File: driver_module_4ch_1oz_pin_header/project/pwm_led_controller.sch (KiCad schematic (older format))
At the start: 35 parts, among them J1 Conn_01x05_Male, J2 Conn_01x02_Male, J3 Conn_01x02_Male, J4 Conn_01x02_Male, J5 Conn_01x02_Male, J6 Conn_01x02_Male, J7 Conn_01x02_Male, U1 AL8843, U2 AL8843, U3 AL8843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

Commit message: Проект выполнен под установку светильника
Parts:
- removed J2, J3: Conn_01x02_Male, my_lib:TerminalBlock-1x02_P5.08mm_Horizontal, symbol Connector:Conn_01x02_Male
- added J2, J3: Conn_01x04_Male, Connector_PinHeader_2.54mm:PinHeader_1x04_P2.54mm_Vertical, symbol Connector:Conn_01x04_Male
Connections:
- net +15V: now also J2.1 (Pin_1), J2.2 (Pin_2)
- net +28V: now also J3.1 (Pin_1), J3.2 (Pin_2)
- net GND: now also J2.3 (Pin_3), J2.4 (Pin_4), J3.3 (Pin_3), J3.4 (Pin_4)
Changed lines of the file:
@@
 L power:+15V #PWR0102
 U 1 1 5C9EEA26
-P 13850 2550
-F 0 "#PWR0102" H 13850 2400 50  0001 C CNN
-F 1 "+15V" H 13865 2723 50  0000 C CNN
-F 2 "" H 13850 2550 50  0001 C CNN
-F 3 "" H 13850 2550 50  0001 C CNN
-	1    13850 2550
+P 15000 2550
+F 0 "#PWR0102" H 15000 2400 50  0001 C CNN
+F 1 "+15V" H 15015 2723 50  0000 C CNN
+F 2 "" H 15000 2550 50  0001 C CNN
+F 3 "" H 15000 2550 50  0001 C CNN
+	1    15000 2550
 	1    0    0    -1
 $EndComp
@@
 L power:GND #PWR0101
 U 1 1 5C9F6278
-P 13850 2650
-F 0 "#PWR0101" H 13850 2400 50  0001 C CNN
-F 1 "GND" H 13855 2477 50  0000 C CNN
-F 2 "" H 13850 2650 50  0001 C CNN
-F 3 "" H 13850 2650 50  0001 C CNN
-	1    13850 2650
+P 15000 2850
+F 0 "#PWR0101" H 15000 2600 50  0001 C CNN
+F 1 "GND" H 15005 2677 50  0000 C CNN
+F 2 "" H 15000 2850 50  0001 C CNN
+F 3 "" H 15000 2850 50  0001 C CNN
+	1    15000 2850
 	1    0    0    -1
 $EndComp
@@
 L power:+28V #PWR0113
 U 1 1 5CA09CB3
-P 13800 3150
-F 0 "#PWR0113" H 13800 3000 50  0001 C CNN
-F 1 "+28V" H 13815 3323 50  0000 C CNN
-F 2 "" H 14050 3200 50  0001 C CNN
-F 3 "" H 14050 3200 50  0001 C CNN
-	1    13800 3150
+P 15000 3600
+F 0 "#PWR0113" H 15000 3450 50  0001 C CNN
+F 1 "+28V" H 15015 3773 50  0000 C CNN
+F 2 "" H 15250 3650 50  0001 C CNN
+F 3 "" H 15250 3650 50  0001 C CNN
+	1    15000 3600
 	1    0    0    -1
 $EndComp
@@
 $EndComp
 $Comp
-L Connector:Conn_01x02_Male J2
-U 1 1 5CA0A8BF
-P 13300 2550
-F 0 "J2" H 13406 2728 50  0000 C CNN
-F 1 "Conn_01x02_Male" H 13406 2637 50  0000 C CNN
-F 2 "my_lib:TerminalBlock-1x02_P5.08mm_Horizontal" H 13300 2550 50  0001 C CNN
-F 3 "~" H 13300 2550 50  0001 C CNN
-	1    13300 2550
-	1    0    0    -1
-$EndComp
-Wire Wire Line
-	13850 2550 13500 2550
-Wire Wire Line
-	13850 2650 13500 2650
-$Comp
-L power:GND #PWR?
+L power:GND #PWR0111
 U 1 1 5CA1B763
-P 13800 3250
-F 0 "#PWR?" H 13800 3000 50  0001 C CNN
-F 1 "GND" H 13805 3077 50  0000 C CNN
-F 2 "" H 13800 3250 50  0001 C CNN
-F 3 "" H 13800 3250 50  0001 C CNN
-	1    13800 3250
-	1    0    0    -1
-$EndComp
-$Comp
-L Connector:Conn_01x02_Male J3
-U 1 1 5CA1B769
-P 13250 3150
-F 0 "J3" H 13356 3328 50  0000 C CNN
-F 1 "Conn_01x02_Male" H 13356 3237 50  0000 C CNN
-F 2 "my_lib:TerminalBlock-1x02_P5.08mm_Horizontal" H 13250 3150 50  0001 C CNN
-F 3 "~" H 13250 3150 50  0001 C CNN
-	1    13250 3150
-	1    0    0    -1
-$EndComp
-Wire Wire Line
-	13800 3150 13450 3150
-Wire Wire Line
-	13800 3250 13450 3250
+P 15000 3900
+F 0 "#PWR0111" H 15000 3650 50  0001 C CNN
+F 1 "GND" H 15005 3727 50  0000 C CNN
+F 2 "" H 15000 3900 50  0001 C CNN
+F 3 "" H 15000 3900 50  0001 C CNN
+	1    15000 3900
+	1    0    0    -1
+$EndComp
+$Comp
+L Connector:Conn_01x04_Male J2
+U 1 1 5CA7A2EA
+P 14300 2650
+F 0 "J2" H 14406 2928 50  0000 C CNN
+F 1 "Conn_01x04_Male" H 14406 2837 50  0000 C CNN
+F 2 "Connector_PinHeader_2.54mm:PinHeader_1x04_P2.54mm_Vertical" H 14300 2650 50  0001 C CNN
+F 3 "~" H 14300 2650 50  0001 C CNN
+	1    14300 2650
+	1    0    0    -1
+$EndComp
+Wire Wire Line
+	15000 2550 14500 2550
+Wire Wire Line
+	14500 2550 14500 2650
+Connection ~ 14500 2550
+Wire Wire Line
+	15000 2850 14500 2850
+Wire Wire Line
+	14500 2850 14500 2750
+Connection ~ 14500 2850
+$Comp
+L Connector:Conn_01x04_Male J3
+U 1 1 5CA82437
+P 14300 3700
+F 0 "J3" H 14406 3978 50  0000 C CNN
+F 1 "Conn_01x04_Male" H 14406 3887 50  0000 C CNN
+F 2 "Connector_PinHeader_2.54mm:PinHeader_1x04_P2.54mm_Vertical" H 14300 3700 50  0001 C CNN
+F 3 "~" H 14300 3700 50  0001 C CNN
+	1    14300 3700
+	1    0    0    -1
+$EndComp
+Wire Wire Line
+	15000 3600 14500 3600
+Wire Wire Line
+	14500 3600 14500 3700
+Connection ~ 14500 3600
+Wire Wire Line
+	15000 3900 14500 3900
+Wire Wire Line
+	14500 3900 14500 3800
+Connection ~ 14500 3900
 $EndSCHEMATC

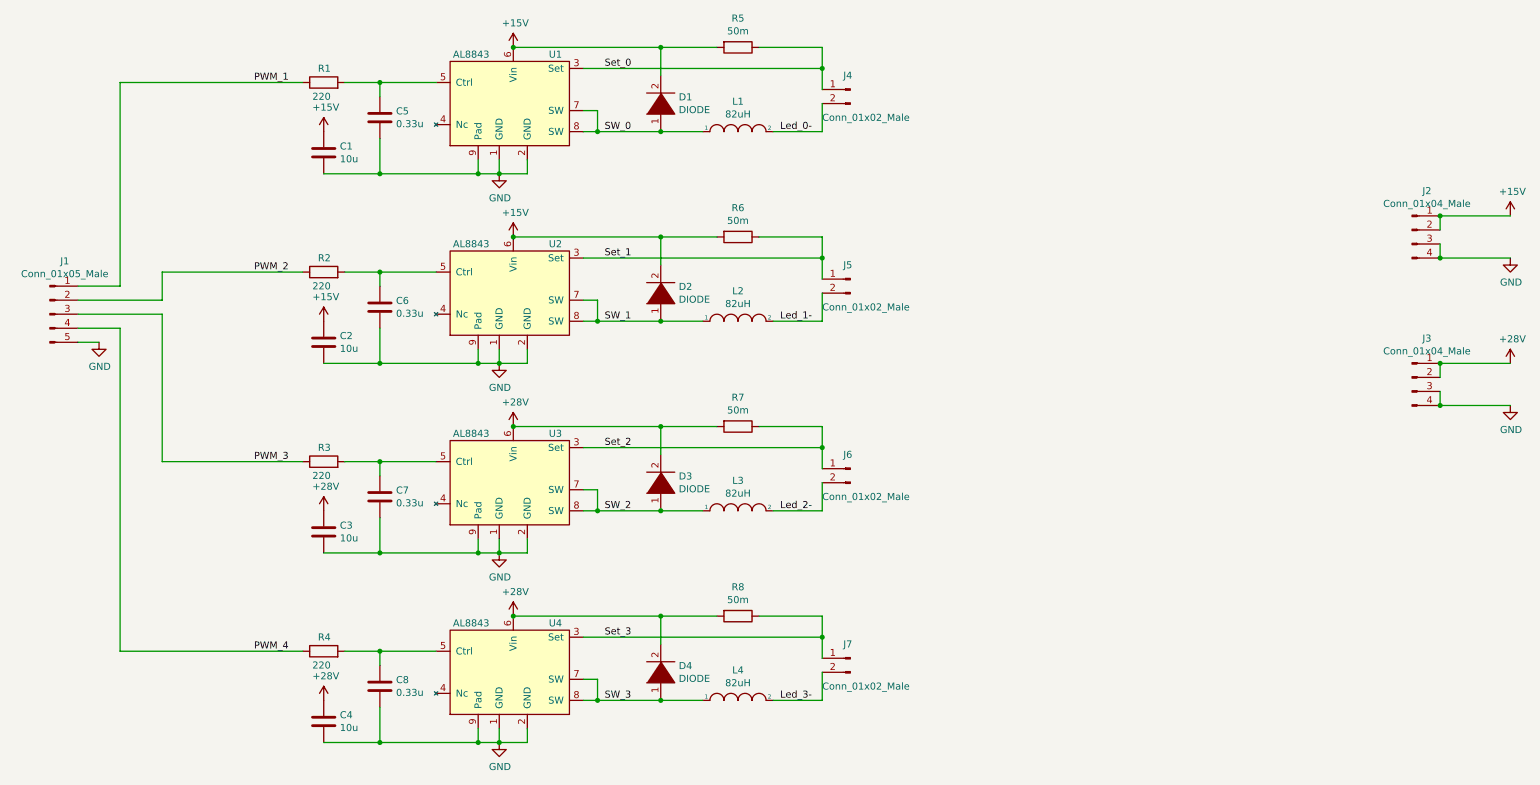
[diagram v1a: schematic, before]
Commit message: Подогнал расположение вилок под светодиодную плату
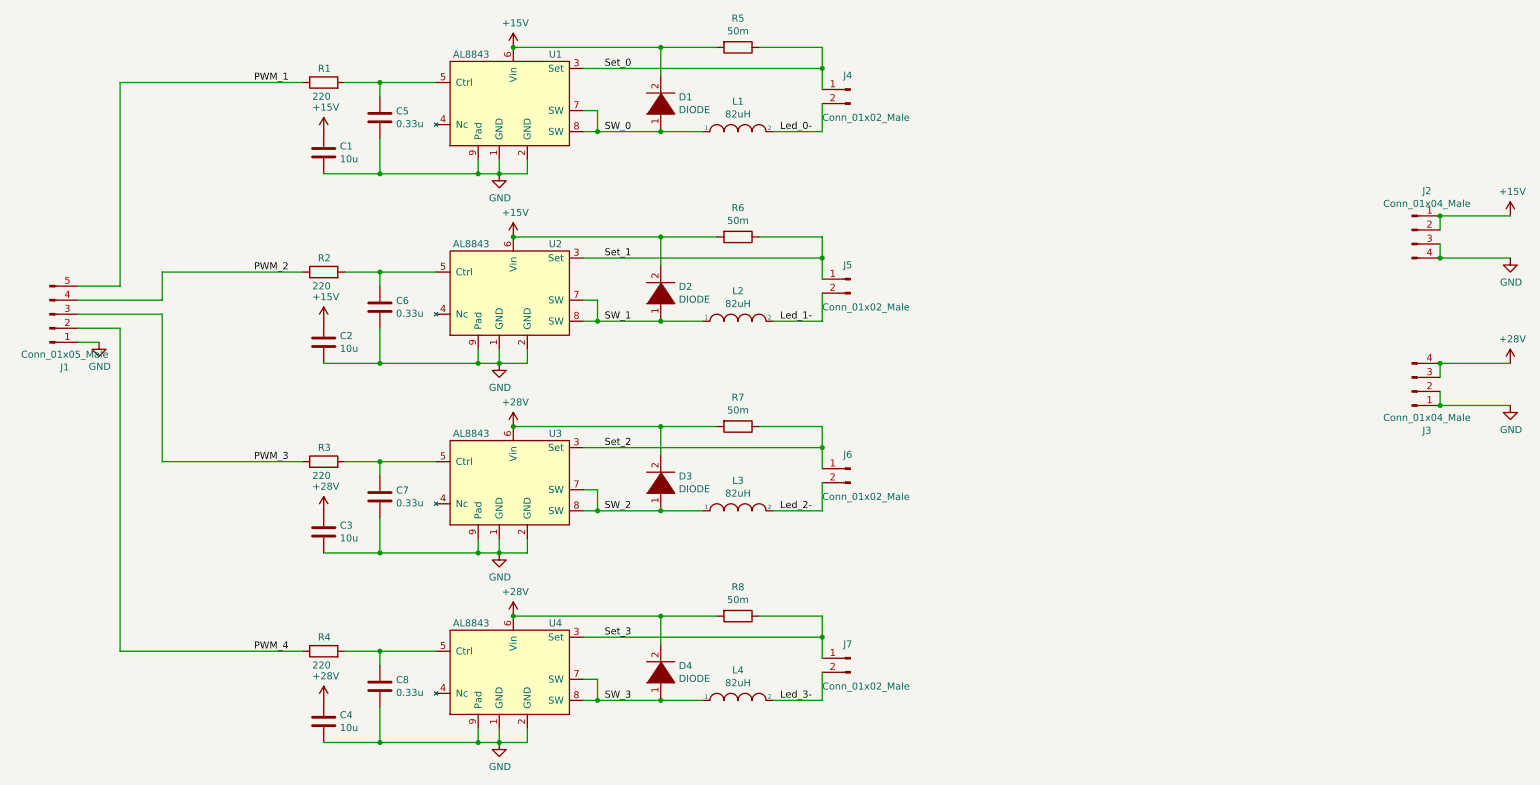
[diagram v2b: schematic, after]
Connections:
- net +28V: now also J3.3 (Pin_3), J3.4 (Pin_4); no longer J3.1 (Pin_1), J3.2 (Pin_2)
- net GND: now also J1.1 (Pin_1), J3.1 (Pin_1), J3.2 (Pin_2); no longer J1.5 (Pin_5), J3.3 (Pin_3), J3.4 (Pin_4)
- net PWM_1: now also J1.5 (Pin_5); no longer J1.1 (Pin_1)
- net PWM_2: now also J1.4 (Pin_4); no longer J1.2 (Pin_2)
- net PWM_4: now also J1.2 (Pin_2); no longer J1.4 (Pin_4)
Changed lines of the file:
@@
 F 3 "~" H 4600 3250 50  0001 C CNN
 	1    4600 3250
-	1    0    0    -1
+	1    0    0    1
 $EndComp
 Wire Wire Line
@@
 L Connector:Conn_01x04_Male J3
 U 1 1 5CA82437
-P 14300 3700
-F 0 "J3" H 14406 3978 50  0000 C CNN
-F 1 "Conn_01x04_Male" H 14406 3887 50  0000 C CNN
-F 2 "Connector_PinHeader_2.54mm:PinHeader_1x04_P2.54mm_Vertical" H 14300 3700 50  0001 C CNN
-F 3 "~" H 14300 3700 50  0001 C CNN
-	1    14300 3700
-	1    0    0    -1
-$EndComp
-Wire Wire Line
+P 14300 3800
+F 0 "J3" H 14406 4078 50  0000 C CNN
+F 1 "Conn_01x04_Male" H 14406 3987 50  0000 C CNN
+F 2 "Connector_PinHeader_2.54mm:PinHeader_1x04_P2.54mm_Vertical" H 14300 3800 50  0001 C CNN
+F 3 "~" H 14300 3800 50  0001 C CNN
+	1    14300 3800
+	1    0    0    1
+$EndComp
+Wire Wire Line
